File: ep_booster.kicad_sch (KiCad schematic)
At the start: 28 parts, among them J1 TB002-500-04BE, Q1 MMBF5457, Q2 BC849C, SW1 SW_DIP_x02

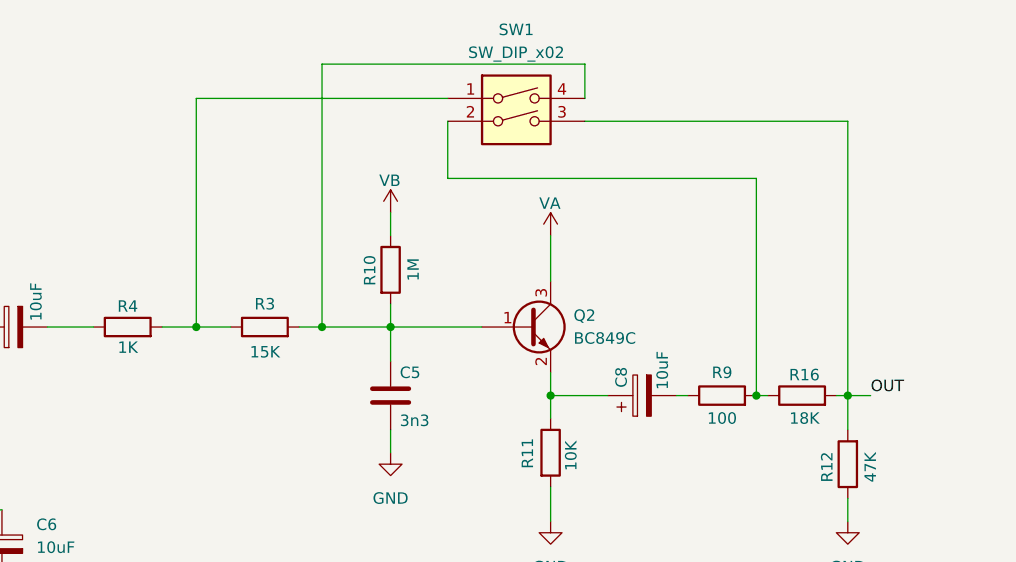
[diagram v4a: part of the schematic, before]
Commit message: changed pot to bourns 3362S
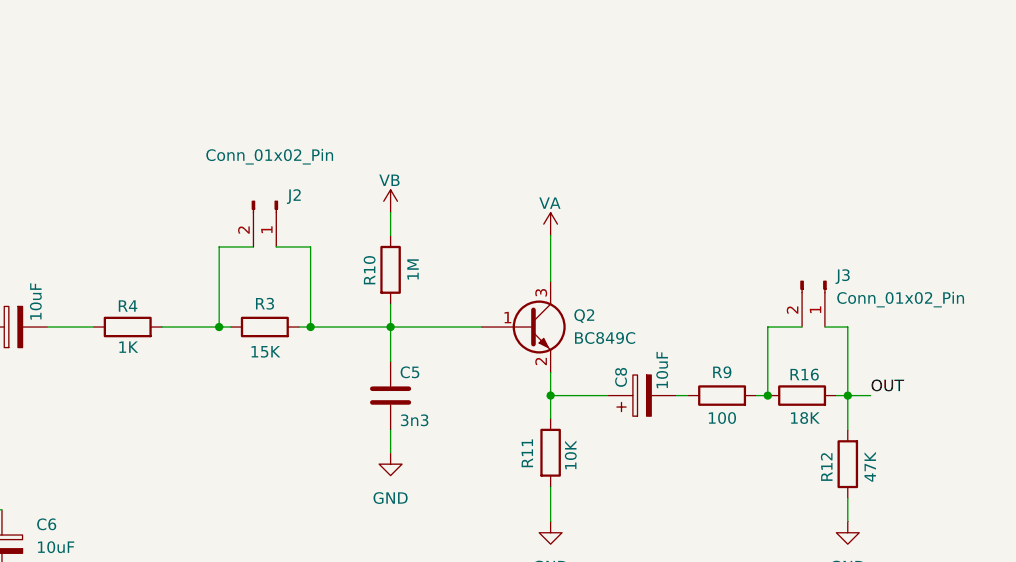
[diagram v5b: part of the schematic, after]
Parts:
- removed SW1: SW_DIP_x02, DS03-254-02BE:DS0325402BE, symbol Switch:SW_DIP_x02
- added J2, J3: Conn_01x02_Pin, Connector_PinHeader_2.54mm:PinHeader_1x02_P2.54mm_Vertical, symbol Connector:Conn_01x02_Pin
- RV1: footprint milos.garunovic:mg_3306K1103 -> footprints:3362S1103LF
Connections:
- net OUT: now also J3.1 (Pin_1)
- net at C5.1, Q2.1 (B), R10.2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: now also J2.1 (Pin_1)
- net at R16.1, R9.2: now also J3.2 (Pin_2)
- net at R3.1, R4.2: now also J2.2 (Pin_2)
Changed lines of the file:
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@@
 	(paper "A4")
+	(junction
+		(at 116.84 44.45)
+		(diameter 0)
+		(color 0 0 0 0)
+	)
 	(junction
 		(at 125.73 44.45)
@@
 	)
 	(junction
-		(at 166.37 52.07)
-		(diameter 0)
-		(color 0 0 0 0)
-	)
-	(junction
 		(at 68.58 44.45)
 		(diameter 0)
@@
 	)
 	(junction
-		(at 143.51 52.07)
+		(at 167.64 52.07)
 		(diameter 0)
 		(color 0 0 0 0)
 	)
 	(junction
-		(at 104.14 44.45)
+		(at 143.51 52.07)
 		(diameter 0)
 		(color 0 0 0 0)
@@
 	)
 	(junction
-		(at 118.11 44.45)
-		(diameter 0)
-		(color 0 0 0 0)
-	)
-	(junction
 		(at 62.23 110.49)
 		(diameter 0)
@@
 	)
 	(junction
+		(at 106.68 44.45)
+		(diameter 0)
+		(color 0 0 0 0)
+	)
+	(junction
 		(at 82.55 73.66)
 		(diameter 0)
@@
 	(wire
 		(pts
+			(xy 116.84 35.56) (xy 116.84 44.45)
+		)
+		(stroke
+			(width 0)
+			(type default)
+		)
+	)
+	(wire
+		(pts
 			(xy 62.23 110.49) (xy 66.04 110.49)
 		)
@@
 	(wire
 		(pts
-			(xy 118.11 15.24) (xy 118.11 44.45)
-		)
-		(stroke
-			(width 0)
-			(type default)
-		)
-	)
-	(wire
-		(pts
 			(xy 176.53 63.5) (xy 176.53 66.04)
 		)
@@
 	(wire
 		(pts
-			(xy 132.08 21.59) (xy 132.08 27.94)
+			(xy 106.68 35.56) (xy 106.68 44.45)
+		)
+		(stroke
+			(width 0)
+			(type default)
+		)
+	)
+	(wire
+		(pts
+			(xy 171.45 44.45) (xy 167.64 44.45)
 		)
 		(stroke
@@
 	(wire
 		(pts
+			(xy 106.68 44.45) (xy 107.95 44.45)
+		)
+		(stroke
+			(width 0)
+			(type default)
+		)
+	)
+	(wire
+		(pts
 			(xy 125.73 58.42) (xy 125.73 55.88)
 		)
@@
 	(wire
 		(pts
-			(xy 115.57 44.45) (xy 118.11 44.45)
-		)
-		(stroke
-			(width 0)
-			(type default)
-		)
-	)
-	(wire
-		(pts
 			(xy 87.63 73.66) (xy 82.55 73.66)
 		)
@@
 	(wire
 		(pts
-			(xy 132.08 19.05) (xy 104.14 19.05)
+			(xy 116.84 44.45) (xy 125.73 44.45)
 		)
 		(stroke
@@
 	(wire
 		(pts
-			(xy 100.33 44.45) (xy 104.14 44.45)
-		)
-		(stroke
-			(width 0)
-			(type default)
-		)
-	)
-	(wire
-		(pts
-			(xy 147.32 21.59) (xy 176.53 21.59)
+			(xy 113.03 35.56) (xy 116.84 35.56)
 		)
 		(stroke
@@
 	(wire
 		(pts
-			(xy 176.53 21.59) (xy 176.53 52.07)
-		)
-		(stroke
-			(width 0)
-			(type default)
-		)
-	)
-	(wire
-		(pts
 			(xy 58.42 66.04) (xy 58.42 69.85)
 		)
@@
 	(wire
 		(pts
+			(xy 176.53 44.45) (xy 173.99 44.45)
+		)
+		(stroke
+			(width 0)
+			(type default)
+		)
+	)
+	(wire
+		(pts
 			(xy 157.48 52.07) (xy 158.75 52.07)
 		)
@@
 	(wire
 		(pts
-			(xy 166.37 27.94) (xy 166.37 52.07)
-		)
-		(stroke
-			(width 0)
-			(type default)
-		)
-	)
-	(wire
-		(pts
 			(xy 73.66 110.49) (xy 77.47 110.49)
 		)
@@
 	(wire
 		(pts
-			(xy 132.08 27.94) (xy 166.37 27.94)
-		)
-		(stroke
-			(width 0)
-			(type default)
-		)
-	)
-	(wire
-		(pts
 			(xy 34.29 54.61) (xy 38.1 54.61)
 		)
@@
 	(wire
 		(pts
-			(xy 147.32 19.05) (xy 147.32 15.24)
-		)
-		(stroke
-			(width 0)
-			(type default)
-		)
-	)
-	(wire
-		(pts
 			(xy 34.29 66.04) (xy 34.29 71.12)
 		)
@@
 	(wire
 		(pts
+			(xy 176.53 52.07) (xy 176.53 44.45)
+		)
+		(stroke
+			(width 0)
+			(type default)
+		)
+	)
+	(wire
+		(pts
 			(xy 62.23 120.65) (xy 62.23 121.92)
 		)
@@
 	(wire
 		(pts
-			(xy 147.32 15.24) (xy 118.11 15.24)
+			(xy 110.49 35.56) (xy 106.68 35.56)
 		)
 		(stroke
@@
 	(wire
 		(pts
-			(xy 104.14 19.05) (xy 104.14 44.45)
-		)
-		(stroke
-			(width 0)
-			(type default)
-		)
-	)
-	(wire
-		(pts
 			(xy 77.47 106.68) (xy 77.47 110.49)
 		)
@@
 	(wire
 		(pts
+			(xy 167.64 44.45) (xy 167.64 52.07)
+		)
+		(stroke
+			(width 0)
+			(type default)
+		)
+	)
+	(wire
+		(pts
 			(xy 68.58 40.64) (xy 68.58 44.45)
 		)
@@
 	(wire
 		(pts
-			(xy 104.14 44.45) (xy 107.95 44.45)
-		)
-		(stroke
-			(width 0)
-			(type default)
-		)
-	)
-	(wire
-		(pts
-			(xy 118.11 44.45) (xy 125.73 44.45)
+			(xy 100.33 44.45) (xy 106.68 44.45)
+		)
+		(stroke
+			(width 0)
+			(type default)
+		)
+	)
+	(wire
+		(pts
+			(xy 115.57 44.45) (xy 116.84 44.45)
 		)
 		(stroke
@@
 	)
 	(symbol
-		(lib_id "Switch:SW_DIP_x02")
-		(at 139.7 21.59 0)
+		(lib_id "Connector:Conn_01x02_Pin")
+		(at 173.99 39.37 270)
 		(unit 1)
 		(exclude_from_sim no)
@@
 		(dnp no)
 		(fields_autoplaced yes)
-		(property "Reference" "SW1"
-			(at 139.7 11.43 0)
-			(effects
-				(font
-					(size 1.27 1.27)
-				)
-			)
-		)
-		(property "Value" "SW_DIP_x02"
-			(at 139.7 13.97 0)
-			(effects
-				(font
-					(size 1.27 1.27)
-				)
-			)
-		)
-		(property "Footprint" "DS03-254-02BE:DS0325402BE"
-			(at 139.7 21.59 0)
+		(property "Reference" "J3"
+			(at 175.26 38.7349 90)
+			(effects
+				(font
+					(size 1.27 1.27)
+				)
+				(justify left)
+			)
+		)
+		(property "Value" "Conn_01x02_Pin"
+			(at 175.26 41.2749 90)
+			(effects
+				(font
+					(size 1.27 1.27)
+				)
+				(justify left)
+			)
+		)
+		(property "Footprint" "Connector_PinHeader_2.54mm:PinHeader_1x02_P2.54mm_Vertical"
+			(at 173.99 39.37 0)
 			(effects
 				(font
@@
 		)
 		(property "Datasheet" "~"
-			(at 139.7 21.59 0)
-			(effects
-				(font
-					(size 1.27 1.27)
-				)
-				(hide yes)
-			)
-		)
-		(property "Description" "2x DIP Switch, Single Pole Single Throw (SPST) switch, small symbol"
-			(at 139.7 21.59 0)
-			(effects
-				(font
-					(size 1.27 1.27)
-				)
-				(hide yes)
-			)
-		)
-		(pin "1"
-		)
-		(pin "4"
+			(at 173.99 39.37 0)
+			(effects
+				(font
+					(size 1.27 1.27)
+				)
+				(hide yes)
+			)
+		)
+		(property "Description" "Generic connector, single row, 01x02, script generated"
+			(at 173.99 39.37 0)
+			(effects
+				(font
+					(size 1.27 1.27)
+				)
+				(hide yes)
+			)
 		)
 		(pin "2"
 		)
-		(pin "3"
-		)
-		(instances
-			(project ""
-				(path "/fa0b5818-9ee4-4073-a6e2-e7b6ccd60214"
-					(reference "SW1")
+		(pin "1"
+		)
+		(instances
+			(project "ep_booster"
+				(path "/fa0b5818-9ee4-4073-a6e2-e7b6ccd60214"
+					(reference "J3")
 					(unit 1)
 				)
@@
 	)
 	(symbol
+		(lib_id "Connector:Conn_01x02_Pin")
+		(at 113.03 30.48 270)
+		(unit 1)
+		(exclude_from_sim no)
+		(in_bom yes)
+		(on_board yes)
+		(dnp no)
+		(property "Reference" "J2"
+			(at 114.3 29.8449 90)
+			(effects
+				(font
+					(size 1.27 1.27)
+				)
+				(justify left)
+			)
+		)
+		(property "Value" "Conn_01x02_Pin"
+			(at 105.156 25.4 90)
+			(effects
+				(font
+					(size 1.27 1.27)
+				)
+				(justify left)
+			)
+		)
+		(property "Footprint" "Connector_PinHeader_2.54mm:PinHeader_1x02_P2.54mm_Vertical"
+			(at 113.03 30.48 0)
+			(effects
+				(font
+					(size 1.27 1.27)
+				)
+				(hide yes)
+			)
+		)
+		(property "Datasheet" "~"
+			(at 113.03 30.48 0)
+			(effects
+				(font
+					(size 1.27 1.27)
+				)
+				(hide yes)
+			)
+		)
+		(property "Description" "Generic connector, single row, 01x02, script generated"
+			(at 113.03 30.48 0)
+			(effects
+				(font
+					(size 1.27 1.27)
+				)
+				(hide yes)
+			)
+		)
+		(pin "2"
+		)
+		(pin "1"
+		)
+		(instances
+			(project ""
+				(path "/fa0b5818-9ee4-4073-a6e2-e7b6ccd60214"
+					(reference "J2")
+					(unit 1)
+				)
+			)
+		)
+	)
+	(symbol
 		(lib_id "Device:C_Polarized")
 		(at 62.23 116.84 0)
@@
 			)
 		)
-		(property "Footprint" "milos.garunovic:mg_3306K1103"
+		(property "Footprint" "footprints:3362S1103LF"
 			(at 82.55 78.74 0)
 			(effects

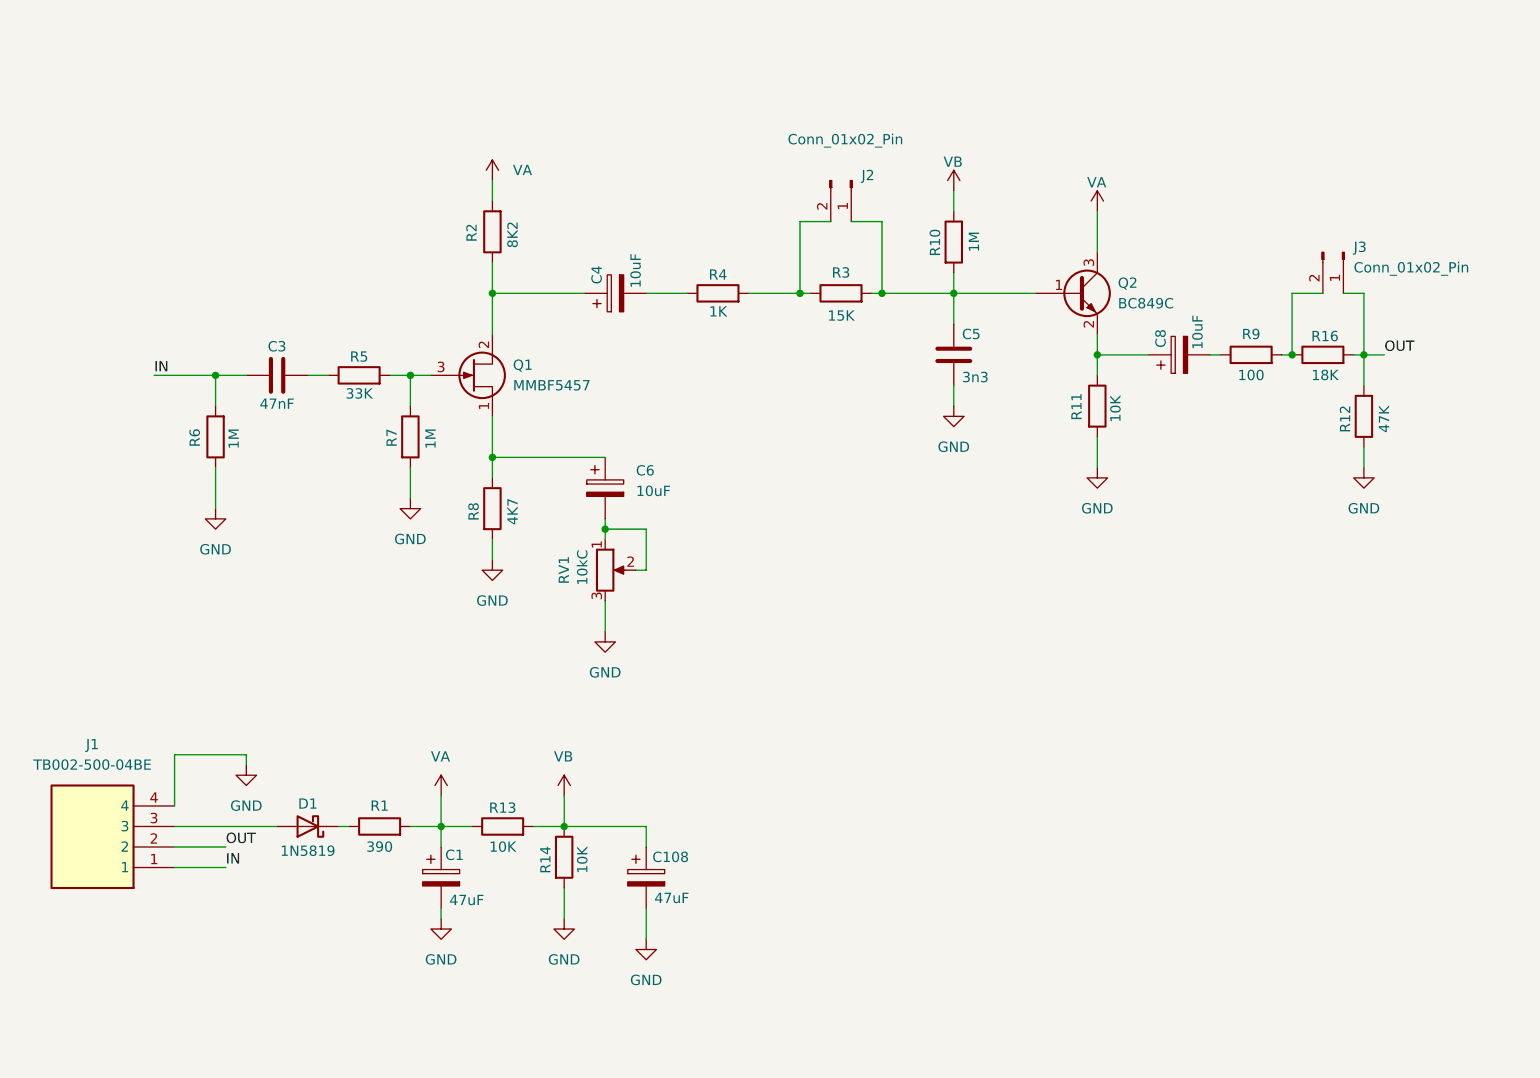
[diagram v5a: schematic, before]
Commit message: schematic design finished according to checklist
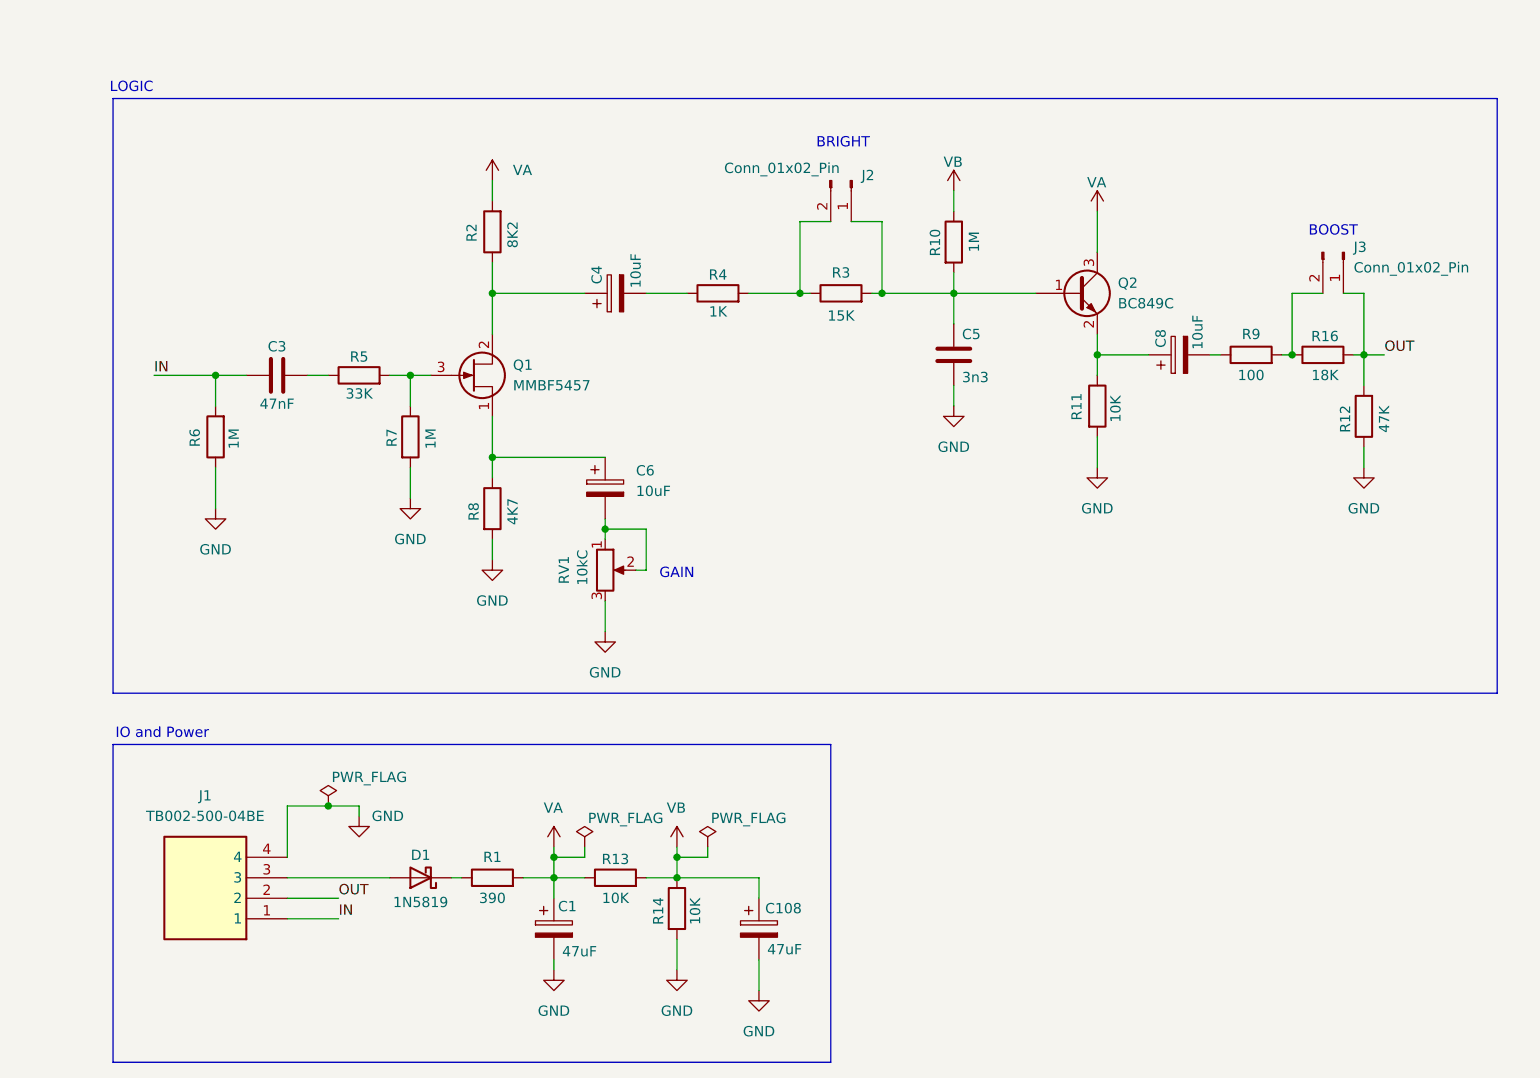
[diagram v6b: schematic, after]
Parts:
- R2: Purpose (none) -> Bias resistor (can be potentiometer) for Q1
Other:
- note added: "BOOST"
- note added: "BRIGHT"
- note added: "GAIN"
- note added: "IO and Power"
- note added: "LOGIC"
- company: (none) -> Miloš Garunović
- title: (none) -> EP Booster
- moved on the sheet: C1, C108, D1, J1, R1, R13, R14

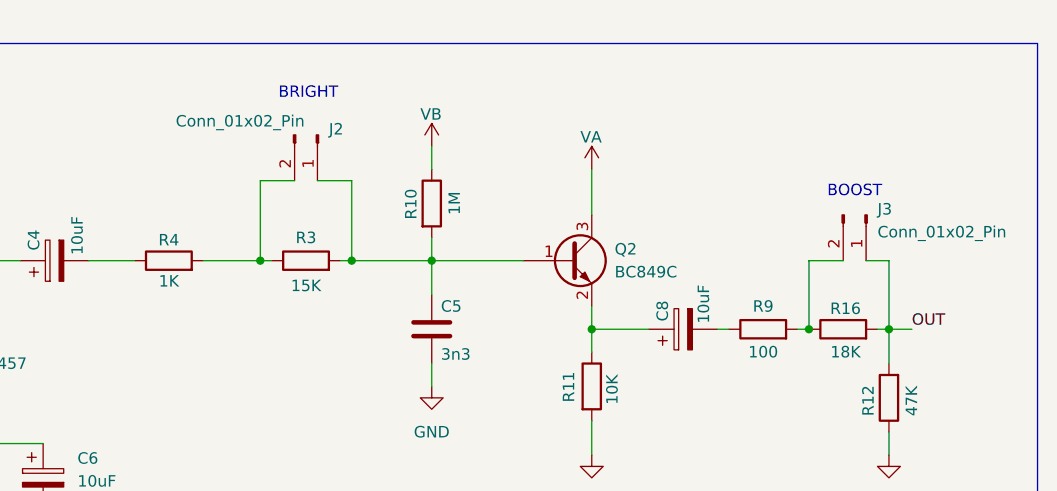
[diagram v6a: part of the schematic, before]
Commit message: replaced two 1x02 pin headers with 1x04
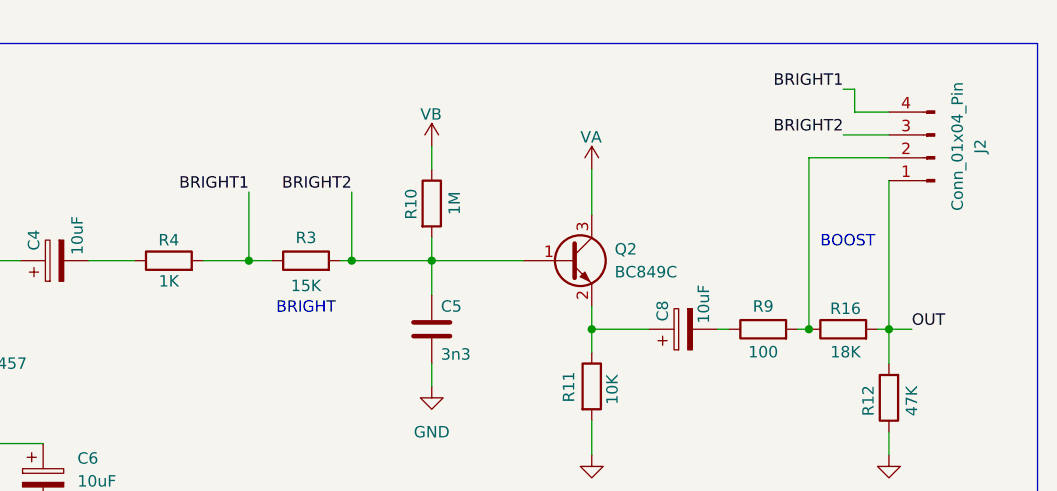
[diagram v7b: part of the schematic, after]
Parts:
- removed J2, J3: Conn_01x02_Pin, Connector_PinHeader_2.54mm:PinHeader_1x02_P2.54mm_Vertical, symbol Connector:Conn_01x02_Pin
- added J2: Conn_01x04_Pin, Connector_PinHeader_2.54mm:PinHeader_1x04_P2.54mm_Vertical, symbol Connector:Conn_01x04_Pin
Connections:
- net OUT: now also J2.1 (Pin_1)
- net BRIGHT2: now reaches C5.1, Q2.1 (B), R10.2, R3.2
- net BRIGHT2: now also J2.3 (Pin_3)
- net at R16.1, R9.2: now also J2.2 (Pin_2)
- net BRIGHT1: now reaches R3.1, R4.2
- net BRIGHT1: now also J2.4 (Pin_4)
